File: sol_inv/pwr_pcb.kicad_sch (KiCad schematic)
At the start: 7 parts, among them J12 IEC_60320_C8_Receptacle, T4 Transformer_1P_1S, U10 AZ1117CR2-3.3

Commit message: v0.2 components change + reference to providers
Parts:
- C28: renamed from C26; ComponentLink2URL (none) -> https://ro.farnell.com/wurth-elektronik/860010275020/cap-22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
- C29: renamed from C27; value 22nF -> 22uF; footprint Capacitor_SMD:C_0805_2012Metric -> Capacitor_SMD:C_1206_3216Metric; ComponentLink2URL (none) -> https://ro.farnell.com/yageo/cc1206kkx5r8bb226/cap-22uf-25v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
- D4: ComponentLink2URL (none) -> https://ro.farnell.com/on-semiconductor/mdb6s/bridge-rectif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
- F1: ComponentLink2URL (none) -> https://ro.farnell.com/multicomp-pro/mc000827/fuse-holder-5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
- J11: renamed from J12; ComponentLink2URL (none) -> https://ro.mouser.com/ProductDetail/Schurter/4300.0103?qs=r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
- T4: symbol Device:Transformer_1P_1S -> Myrra 44229:44230; ComponentLink2URL (none) -> https://ro.farnell.com/myrra/44229/transformer-5va-6v/dp/16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
- U10: ComponentLink2URL (none) -> https://ro.farnell.com/diodes-inc/az1117cr2-3-3trg1/ldo-dc-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
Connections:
- net at J11.2 (N): now also T4.6; no longer T4.2 (AB)
- net at D4.3: now also T4.8; no longer T4.3 (SA)
- net at F1.1: now also T4.11; no longer T4.4 (SB)
- no-connect marks 0 -> 2
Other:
- moved on the sheet: C28, C29, D4, F1, J11, U10

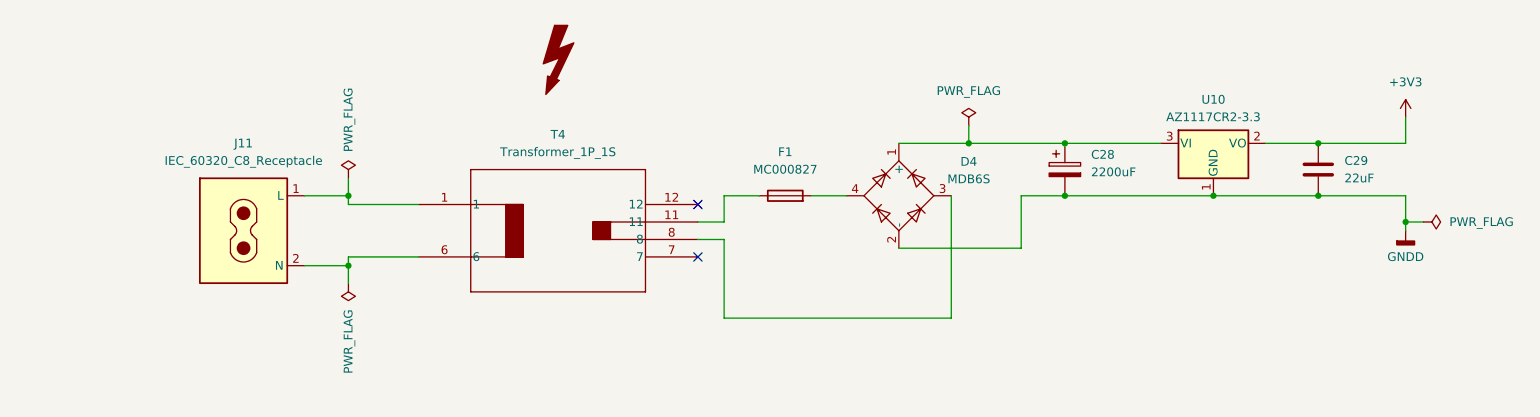
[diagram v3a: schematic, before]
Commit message: v0.3.4 fixes + component change for farnell
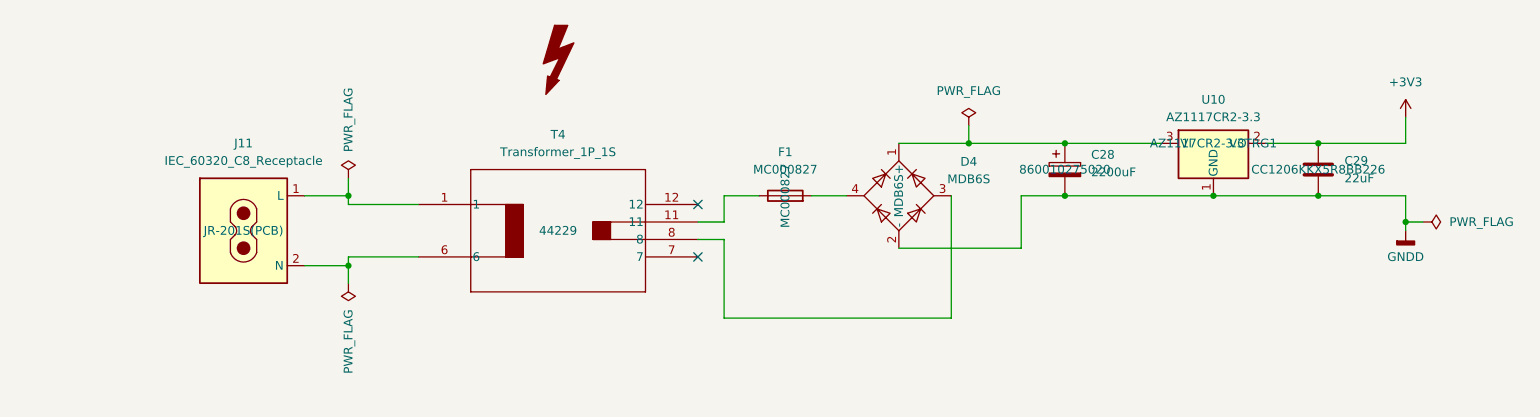
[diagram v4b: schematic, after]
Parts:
- C28: Manufacturer Part Number (none) -> 860010275020
- C29: Manufacturer Part Number (none) -> CC1206KKX5R8BB226
- D4: Manufacturer Part Number (none) -> MDB6S
- F1: Manufacturer Part Number (none) -> MC000827
- J11: ComponentLink2URL https://ro.mouser.com/ProductDetail/Schurter/4300.0103?qs=r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 -> https://ro.farnell.com/multicomp-pro/jr-201s-pcb/inlet-iec-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; Manufacturer Part Number (none) -> JR-201S(PCB)
- T4: Manufacturer Part Number (none) -> 44229
- U10: Manufacturer Part Number (none) -> AZ1117CR2-3.3TRG1
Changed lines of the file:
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@@
 	(title_block
 		(title "PCB Power Source")
-		(date "2025-05-01")
-		(rev "0.3")
+		(date "2025-05-26")
+		(rev "0.3.1")
 		(company "Cezar-Octavian Bontaș")
 	)
@@
 			)
 		)
+		(property "Manufacturer Part Number" "CC1206KKX5R8BB226"
+			(at 228.6 107.95 0)
+			(effects
+				(font
+					(size 1.27 1.27)
+				)
+			)
+		)
 		(pin "1"
 		)
@@
 			)
 		)
+		(property "Manufacturer Part Number" "AZ1117CR2-3.3TRG1"
+			(at 213.36 104.14 0)
+			(effects
+				(font
+					(size 1.27 1.27)
+				)
+			)
+		)
 		(pin "2"
 		)
@@
 			)
 		)
+		(property "Manufacturer Part Number" "44229"
+			(at 118.11 116.84 0)
+			(effects
+				(font
+					(size 1.27 1.27)
+				)
+			)
+		)
 		(pin "8"
 		)
@@
 			)
 		)
+		(property "Manufacturer Part Number" "MDB6S"
+			(at 167.64 111.76 0)
+			(effects
+				(font
+					(size 1.27 1.27)
+				)
+			)
+		)
 		(pin "4"
 		)
@@
 			)
 		)
-		(property "Datasheet" "https://ro.mouser.com/datasheet/2/358/typ_2570-1283887.pdf"
+		(property "Datasheet" "https://www.farnell.com/datasheets/3186237.pdf"
 			(at 72.39 116.84 0)
 			(effects
@@
 			)
 		)
-		(property "ComponentLink2URL" "https://ro.mouser.com/ProductDetail/Schurter/4300.0103?qs=rrS6PyfT74fALdoccvhz1Q%3D%3D"
+		(property "ComponentLink2URL" "https://ro.farnell.com/multicomp-pro/jr-201s-pcb/inlet-iec-class2-fig-8-pcb/dp/9248161"
 			(at 72.39 116.84 0)
 			(effects
@@
 				)
 				(hide yes)
+			)
+		)
+		(property "Manufacturer Part Number" "JR-201S(PCB)"
+			(at 72.39 116.84 0)
+			(effects
+				(font
+					(size 1.27 1.27)
+				)
 			)
 		)
@@
 			)
 		)
+		(property "Manufacturer Part Number" "MC000827"
+			(at 151.13 111.76 0)
+			(effects
+				(font
+					(size 1.27 1.27)
+				)
+			)
+		)
 		(pin "1"
 		)
@@
 			)
 		)
+		(property "Manufacturer Part Number" "860010275020"
+			(at 191.77 107.95 0)
+			(effects
+				(font
+					(size 1.27 1.27)
+				)
+			)
+		)

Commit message: v0.4 fixed mcu ldo part, production testing
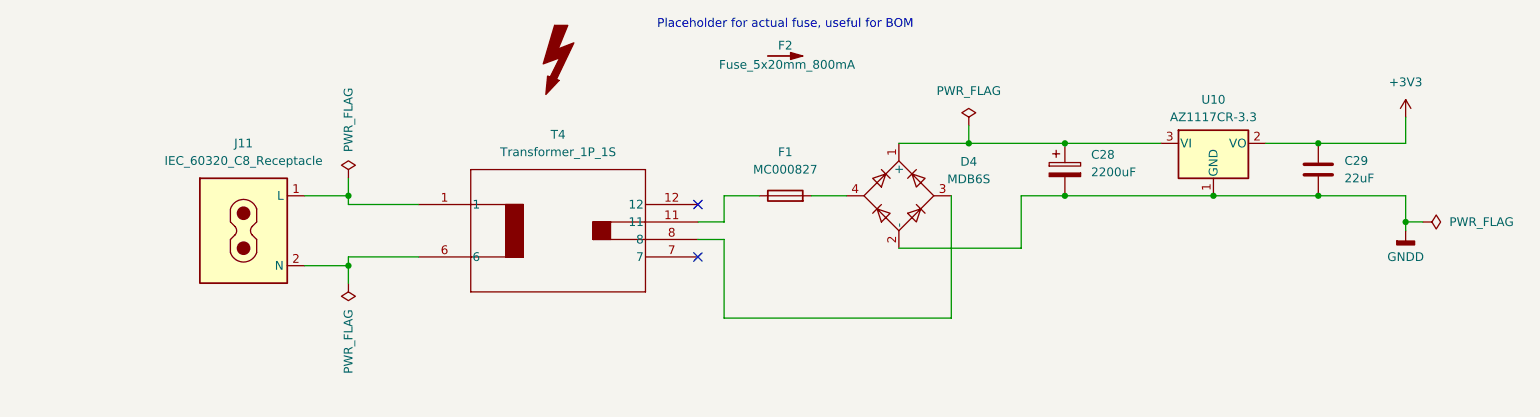
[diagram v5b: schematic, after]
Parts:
- added F2: Fuse_5x20mm_800mA, symbol Graphic:SYM_Arrow_Normal
- U10: value AZ1117CR2-3.3 -> AZ1117CR-3.3; ComponentLink2URL https://ro.farnell.com/diodes-inc/az1117cr2-3-3trg1/ldo-dc-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 -> https://ro.farnell.com/diodes-inc/az1117cr-3-3trg1/ldo-fixe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
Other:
- note added: "Placeholder for actual fuse, useful for BOM"
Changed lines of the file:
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@@
 	(title_block
 		(title "PCB Power Source")
-		(date "2025-05-26")
-		(rev "0.3.1")
+		(date "2025-07-29")
+		(rev "0.4")
 		(company "Cezar-Octavian Bontaș")
+	)
+	(text "Placeholder for actual fuse, useful for BOM"
+		(exclude_from_sim yes)
+		(at 151.13 86.868 0)
+		(effects
+			(font
+				(size 1.27 1.27)
+			)
+		)
 	)
 	(junction
@@
 					(size 1.27 1.27)
 				)
+				(hide yes)
+			)
+		)
+		(property "Sim.Enable" ""
+			(at 228.6 107.95 0)
+			(effects
+				(font
+					(size 1.27 1.27)
+				)
 			)
 		)
@@
 			)
 		)
-		(property "Value" "AZ1117CR2-3.3"
+		(property "Value" "AZ1117CR-3.3"
 			(at 213.36 100.33 0)
 			(effects
@@
 			)
 		)
-		(property "ComponentLink2URL" "https://ro.farnell.com/diodes-inc/az1117cr2-3-3trg1/ldo-dc-dc-conv-3-3v-0-8a-sot-89/dp/3942513"
+		(property "ComponentLink2URL" "https://ro.farnell.com/diodes-inc/az1117cr-3-3trg1/ldo-fixed-3-3v-0-8a-20-to-125deg/dp/3483076"
 			(at 213.36 104.14 0)
 			(effects
@@
 		)
 		(property "Manufacturer Part Number" "AZ1117CR2-3.3TRG1"
+			(at 213.36 104.14 0)
+			(effects
+				(font
+					(size 1.27 1.27)
+				)
+				(hide yes)
+			)
+		)
+		(property "Sim.Enable" ""
 			(at 213.36 104.14 0)
 			(effects
@@
 				(path "/c5b733d3-d844-4c5a-a928-539beea9cfbc/55c49600-108e-423a-878a-ddd218e994fd"
 					(reference "U10")
+					(unit 1)
+				)
+			)
+		)
+	)
+	(symbol
+		(lib_id "Graphic:SYM_Arrow_Normal")
+		(at 151.13 91.44 0)
+		(unit 1)
+		(exclude_from_sim yes)
+		(in_bom yes)
+		(on_board no)
+		(dnp no)
+		(fields_autoplaced yes)
+		(property "Reference" "F2"
+			(at 151.13 89.916 0)
+			(effects
+				(font
+					(size 1.27 1.27)
+				)
+			)
+		)
+		(property "Value" "Fuse_5x20mm_800mA"
+			(at 151.384 92.71 0)
+			(effects
+				(font
+					(size 1.27 1.27)
+				)
+			)
+		)
+		(property "Footprint" ""
+			(at 151.13 91.44 0)
+			(effects
+				(font
+					(size 1.27 1.27)
+				)
+				(hide yes)
+			)
+		)
+		(property "Datasheet" "https://www.farnell.com/datasheets/2842926.pdf"
+			(at 151.13 91.44 0)
+			(effects
+				(font
+					(size 1.27 1.27)
+				)
+				(hide yes)
+			)
+		)
+		(property "Description" "Filled arrow, 200mil"
+			(at 151.13 91.44 0)
+			(effects
+				(font
+					(size 1.27 1.27)
+				)
+				(hide yes)
+			)
+		)
+		(property "ComponentLink2URL" "https://ro.farnell.com/multicomp-pro/mp000851/fuse-cartridge-time-delay-0-8a/dp/3220873"
+			(at 151.13 91.44 0)
+			(effects
+				(font
+					(size 1.27 1.27)
+				)
+				(hide yes)
+			)
+		)
+		(property "Manufacturer Part Number" "MP000851"
+			(at 151.13 91.44 0)
+			(effects
+				(font
+					(size 1.27 1.27)
+				)
+				(hide yes)
+			)
+		)
+		(property "Sim.Enable" ""
+			(at 151.13 91.44 0)
+			(effects
+				(font
+					(size 1.27 1.27)
+				)
+			)
+		)
+		(instances
+			(project ""
+				(path "/c5b733d3-d844-4c5a-a928-539beea9cfbc/55c49600-108e-423a-878a-ddd218e994fd"
+					(reference "F2")
 					(unit 1)
 				)
@@
 					(size 1.27 1.27)
 				)
+				(hide yes)
+			)
+		)
+		(property "Sim.Enable" ""
+			(at 118.11 116.84 0)
+			(effects
+				(font
+					(size 1.27 1.27)
+				)
 			)
 		)
@@
 					(size 1.27 1.27)
 				)
+				(hide yes)
+			)
+		)
+		(property "Sim.Enable" ""
+			(at 167.64 111.76 0)
+			(effects
+				(font
+					(size 1.27 1.27)
+				)
 			)
 		)
@@
 					(size 1.27 1.27)
 				)
+				(hide yes)
+			)
+		)
+		(property "Sim.Enable" ""
+			(at 72.39 116.84 0)
+			(effects
+				(font
+					(size 1.27 1.27)
+				)
 			)
 		)
@@
 					(size 1.27 1.27)
 				)
+				(hide yes)
+			)
+		)
+		(property "Sim.Enable" ""
+			(at 151.13 111.76 0)
+			(effects
+				(font
+					(size 1.27 1.27)
+				)
 			)
 		)
@@
 			(at 191.77 107.95 0)
 			(effects
+				(font
+					(size 1.27 1.27)
+				)
+				(hide yes)
+			)
+		)
+		(property "Sim.Enable" ""
+			(at 191.77 107.95 0)
+			(effects
